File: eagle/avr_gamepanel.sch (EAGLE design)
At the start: 181 parts, among them IC1 74HCT14N, IC10 74HC165N, IC11 ATMEGA328P, IC2 74HCT14N, IC3 74HCT14N, IC4 74HCT14N, IC5 74HCT14N, IC6 74HCT14N, IC7 74HC165N, IC8 74HC165N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

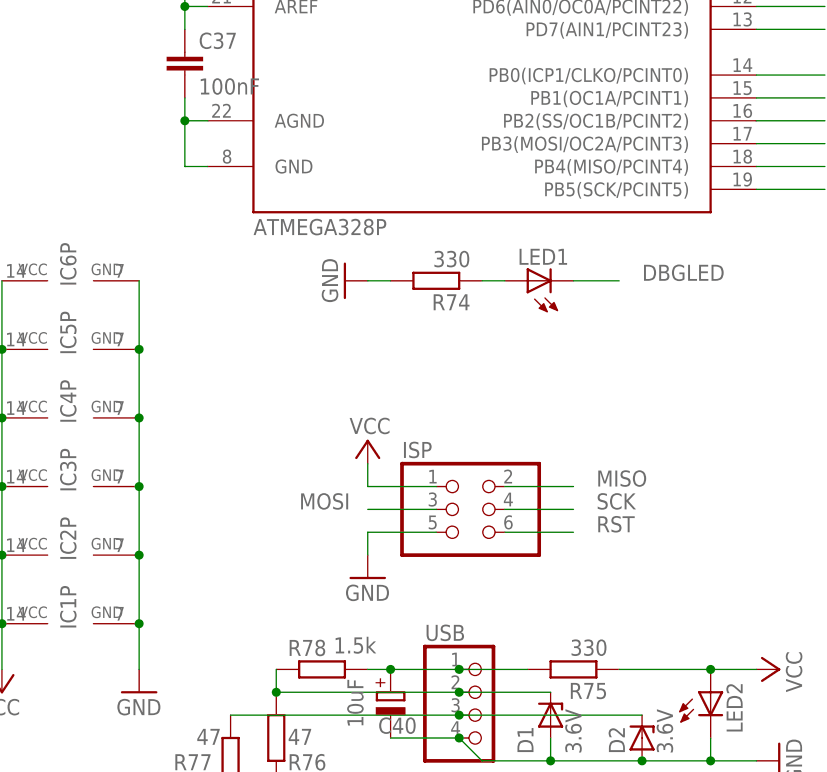
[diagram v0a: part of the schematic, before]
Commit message: fixed two minor circuitry errors
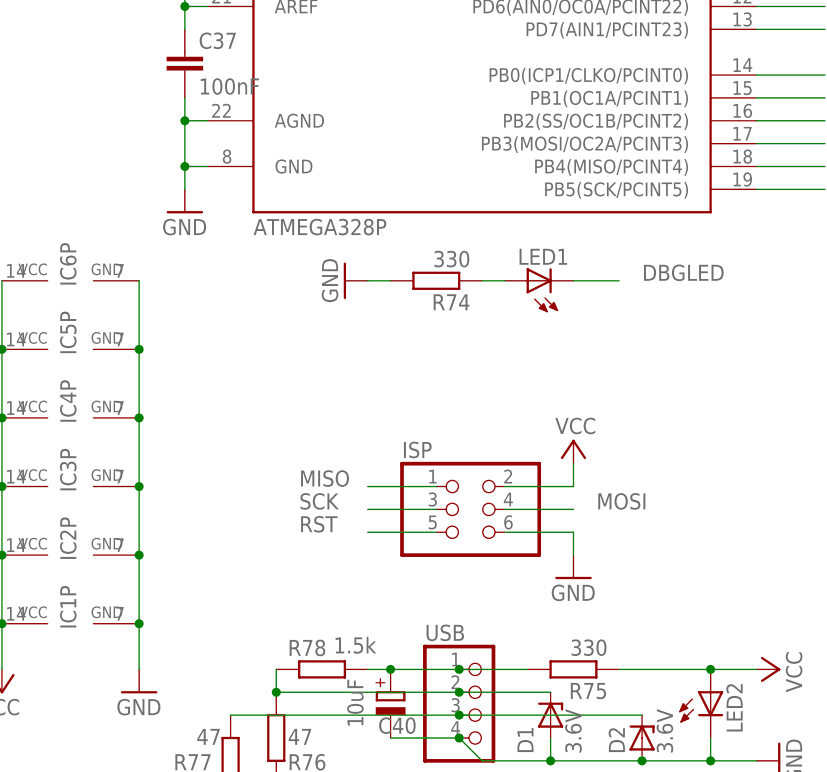
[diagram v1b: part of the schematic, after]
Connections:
- removed net N$113: C37.2, IC11.AGND, IC11.GND@1
- net GND: now also C37.2, IC11.AGND, IC11.GND@1, ISP.6; no longer ISP.5
- net MISO: now also ISP.1; no longer ISP.2
- net MOSI: now also ISP.4; no longer ISP.3
- net RST: now also ISP.5; no longer ISP.6
- net SCK: now also ISP.3; no longer ISP.4
- net VCC: now also ISP.2; no longer ISP.1
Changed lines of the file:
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@@
 <part name="GND12" library="supply1" deviceset="GND" device=""/>
 <part name="P+11" library="supply1" deviceset="VCC" device=""/>
+<part name="GND13" library="supply1" deviceset="GND" device=""/>
 </parts>
 <sheets>
@@
 <attribute name="VALUE" x="294.64" y="144.78" size="1.778" layer="96" rot="R270"/>
 </instance>
-<instance part="P+7" gate="VCC" x="322.58" y="88.9" smashed="yes">
-<attribute name="VALUE" x="325.12" y="91.44" size="1.778" layer="96" rot="R180"/>
-</instance>
-<instance part="GND9" gate="1" x="322.58" y="73.66" smashed="yes">
-<attribute name="VALUE" x="320.04" y="71.12" size="1.778" layer="96"/>
+<instance part="P+7" gate="VCC" x="345.44" y="88.9" smashed="yes">
+<attribute name="VALUE" x="347.98" y="91.44" size="1.778" layer="96" rot="R180"/>
+</instance>
+<instance part="GND9" gate="1" x="345.44" y="73.66" smashed="yes">
+<attribute name="VALUE" x="342.9" y="71.12" size="1.778" layer="96"/>
 </instance>
 <instance part="JRZ" gate="A" x="350.52" y="243.84" rot="R90"/>
@@
 <instance part="P+11" gate="VCC" x="10.16" y="215.9" smashed="yes" rot="R180">
 <attribute name="VALUE" x="7.62" y="213.36" size="1.778" layer="96"/>
+</instance>
+<instance part="GND13" gate="1" x="302.26" y="114.3" smashed="yes">
+<attribute name="VALUE" x="299.72" y="111.76" size="1.778" layer="96"/>
 </instance>
 </instances>
@@
 </segment>
 <segment>
-<pinref part="ISP" gate="A" pin="1"/>
-<wire x1="330.2" y1="83.82" x2="322.58" y2="83.82" width="0.1524" layer="91"/>
-<pinref part="P+7" gate="VCC" pin="VCC"/>
-<wire x1="322.58" y1="86.36" x2="322.58" y2="83.82" width="0.1524" layer="91"/>
-</segment>
-<segment>
 <pinref part="JX" gate="A" pin="2"/>
 <pinref part="JY" gate="A" pin="2"/>
@@
 <wire x1="10.16" y1="241.3" x2="10.16" y2="248.92" width="0.1524" layer="91"/>
 <junction x="10.16" y="241.3"/>
+</segment>
+<segment>
+<pinref part="ISP" gate="A" pin="2"/>
+<wire x1="337.82" y1="83.82" x2="345.44" y2="83.82" width="0.1524" layer="91"/>
+<pinref part="P+7" gate="VCC" pin="VCC"/>
+<wire x1="345.44" y1="83.82" x2="345.44" y2="86.36" width="0.1524" layer="91"/>
 </segment>
 </net>
@@
 </segment>
 <segment>
-<pinref part="ISP" gate="A" pin="5"/>
-<wire x1="330.2" y1="78.74" x2="322.58" y2="78.74" width="0.1524" layer="91"/>
-<pinref part="GND9" gate="1" pin="GND"/>
-<wire x1="322.58" y1="76.2" x2="322.58" y2="78.74" width="0.1524" layer="91"/>
-</segment>
-<segment>
 <pinref part="JRZ" gate="A" pin="3"/>
 <pinref part="JRY" gate="A" pin="3"/>
@@
 <wire x1="25.4" y1="241.3" x2="25.4" y2="248.92" width="0.1524" layer="91"/>
 <junction x="25.4" y="241.3"/>
+</segment>
+<segment>
+<pinref part="IC11" gate="1" pin="AGND"/>
+<pinref part="C37" gate="G$1" pin="2"/>
+<wire x1="304.8" y1="124.46" x2="302.26" y2="124.46" width="0.1524" layer="91"/>
+<wire x1="302.26" y1="124.46" x2="302.26" y2="127" width="0.1524" layer="91"/>
+<pinref part="IC11" gate="1" pin="GND@1"/>
+<wire x1="304.8" y1="119.38" x2="302.26" y2="119.38" width="0.1524" layer="91"/>
+<wire x1="302.26" y1="119.38" x2="302.26" y2="124.46" width="0.1524" layer="91"/>
+<junction x="302.26" y="124.46"/>
+<pinref part="GND13" gate="1" pin="GND"/>
+<wire x1="302.26" y1="116.84" x2="302.26" y2="119.38" width="0.1524" layer="91"/>
+<junction x="302.26" y="119.38"/>
+</segment>
+<segment>
+<pinref part="ISP" gate="A" pin="6"/>
+<wire x1="337.82" y1="78.74" x2="345.44" y2="78.74" width="0.1524" layer="91"/>
+<pinref part="GND9" gate="1" pin="GND"/>
+<wire x1="345.44" y1="78.74" x2="345.44" y2="76.2" width="0.1524" layer="91"/>
 </segment>
 </net>
@@
 </segment>
 </net>
-<net name="N$113" class="0">
-<segment>
-<pinref part="IC11" gate="1" pin="AGND"/>
-<pinref part="C37" gate="G$1" pin="2"/>
-<wire x1="304.8" y1="124.46" x2="302.26" y2="124.46" width="0.1524" layer="91"/>
-<wire x1="302.26" y1="124.46" x2="302.26" y2="127" width="0.1524" layer="91"/>
-<pinref part="IC11" gate="1" pin="GND@1"/>
-<wire x1="304.8" y1="119.38" x2="302.26" y2="119.38" width="0.1524" layer="91"/>
-<wire x1="302.26" y1="119.38" x2="302.26" y2="124.46" width="0.1524" layer="91"/>
-<junction x="302.26" y="124.46"/>
-</segment>
-</net>
 <net name="N$116" class="0">
 <segment>
@@
 </net>
 <net name="MOSI" class="0">
-<segment>
-<pinref part="IC11" gate="1" pin="PB3(MOSI/OC2A/PCINT3)"/>
-<wire x1="365.76" y1="121.92" x2="373.38" y2="121.92" width="0.1524" layer="91"/>
-<label x="375.92" y="121.92" size="1.778" layer="95"/>
-</segment>
 <segment>
 <pinref part="IC7" gate="A" pin="SH/!LD"/>
@@
 </segment>
 <segment>
-<pinref part="ISP" gate="A" pin="3"/>
-<wire x1="330.2" y1="81.28" x2="322.58" y2="81.28" width="0.1524" layer="91"/>
-<label x="314.96" y="81.28" size="1.778" layer="95"/>
-</segment>
-</net>
-<net name="MISO" class="0">
-<segment>
-<pinref part="ISP" gate="A" pin="2"/>
-<wire x1="337.82" y1="83.82" x2="345.44" y2="83.82" width="0.1524" layer="91"/>
-<label x="347.98" y="83.82" size="1.778" layer="95"/>
-</segment>
-<segment>
-<pinref part="IC11" gate="1" pin="PB4(MISO/PCINT4)"/>
-<wire x1="365.76" y1="119.38" x2="373.38" y2="119.38" width="0.1524" layer="91"/>
-<label x="375.92" y="119.38" size="1.778" layer="95"/>
-</segment>
-</net>
-<net name="SCK" class="0">
+<pinref part="IC11" gate="1" pin="PB3(MOSI/OC2A/PCINT3)"/>
+<wire x1="365.76" y1="121.92" x2="373.38" y2="121.92" width="0.1524" layer="91"/>
+<label x="375.92" y="121.92" size="1.778" layer="95"/>
+</segment>
 <segment>
 <pinref part="ISP" gate="A" pin="4"/>
@@
 <label x="347.98" y="81.28" size="1.778" layer="95"/>
 </segment>
-<segment>
-<pinref part="IC11" gate="1" pin="PB5(SCK/PCINT5)"/>
-<wire x1="365.76" y1="116.84" x2="373.38" y2="116.84" width="0.1524" layer="91"/>
-<label x="375.92" y="116.84" size="1.778" layer="95"/>
-</segment>
 </net>
 <net name="RST" class="0">
-<segment>
-<pinref part="ISP" gate="A" pin="6"/>
-<wire x1="337.82" y1="78.74" x2="345.44" y2="78.74" width="0.1524" layer="91"/>
-<label x="347.98" y="78.74" size="1.778" layer="95"/>
-</segment>
 <segment>
 <pinref part="RST1" gate="1" pin="S1"/>
@@
 <wire x1="302.26" y1="182.88" x2="304.8" y2="182.88" width="0.1524" layer="91"/>
 </segment>
+<segment>
+<pinref part="ISP" gate="A" pin="5"/>
+<wire x1="330.2" y1="78.74" x2="322.58" y2="78.74" width="0.1524" layer="91"/>
+<label x="314.96" y="78.74" size="1.778" layer="95"/>
+</segment>
 </net>
 <net name="J_AX_X" class="0">
@@
 </segment>
 </net>
+<net name="MISO" class="0">
+<segment>
+<pinref part="IC11" gate="1" pin="PB4(MISO/PCINT4)"/>
+<wire x1="365.76" y1="119.38" x2="373.38" y2="119.38" width="0.1524" layer="91"/>
+<label x="375.92" y="119.38" size="1.778" layer="95"/>
+</segment>
+<segment>
+<pinref part="ISP" gate="A" pin="1"/>
+<wire x1="330.2" y1="83.82" x2="322.58" y2="83.82" width="0.1524" layer="91"/>
+<label x="314.96" y="83.82" size="1.778" layer="95"/>
+</segment>
+</net>
+<net name="SCK" class="0">
+<segment>
+<pinref part="IC11" gate="1" pin="PB5(SCK/PCINT5)"/>
+<wire x1="365.76" y1="116.84" x2="373.38" y2="116.84" width="0.1524" layer="91"/>
+<label x="375.92" y="116.84" size="1.778" layer="95"/>
+</segment>
+<segment>
+<pinref part="ISP" gate="A" pin="3"/>
+<wire x1="330.2" y1="81.28" x2="322.58" y2="81.28" width="0.1524" layer="91"/>
+<label x="314.96" y="81.28" size="1.778" layer="95"/>
+</segment>
+</net>
